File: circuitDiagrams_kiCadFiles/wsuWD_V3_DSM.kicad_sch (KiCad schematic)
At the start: 33 parts, among them J1 Conn_01x04_Male, J2 Screw Terminal, U1 MCP2561-E-P, U2 LD1086DT50TR, U3 ATmega644A-P, U7 MAX7219, U8 MCP2515-xSO, X1 ACO-20MHz-A

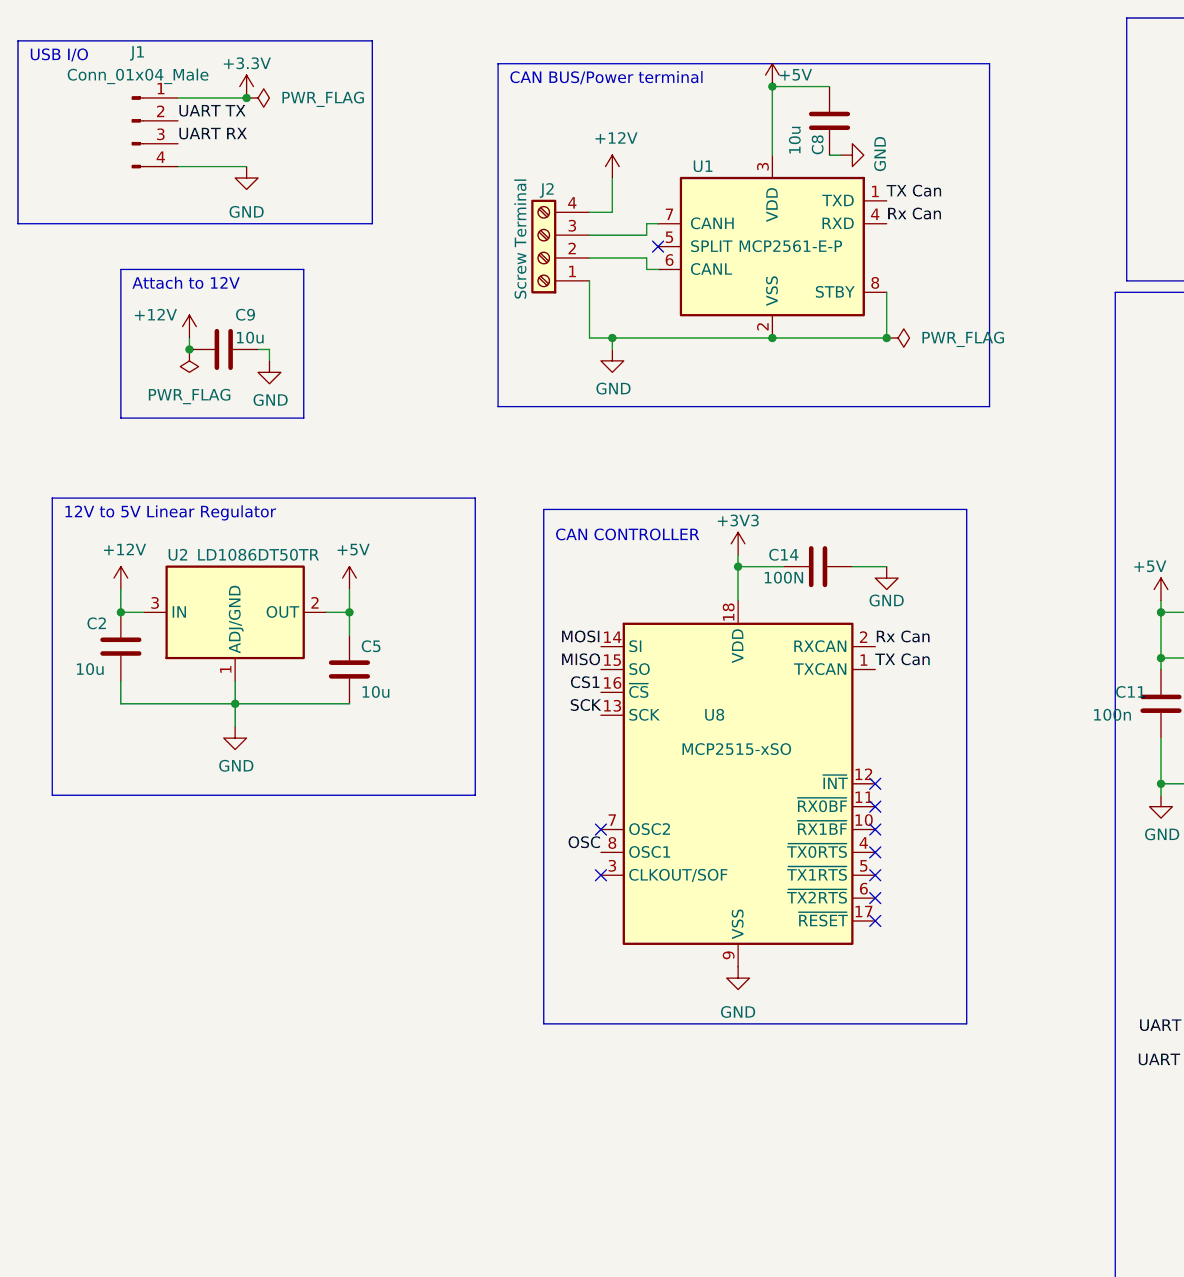
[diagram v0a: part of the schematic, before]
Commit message: Added BOB to schematic
Added BOB to schematic
Now ready for pcb design
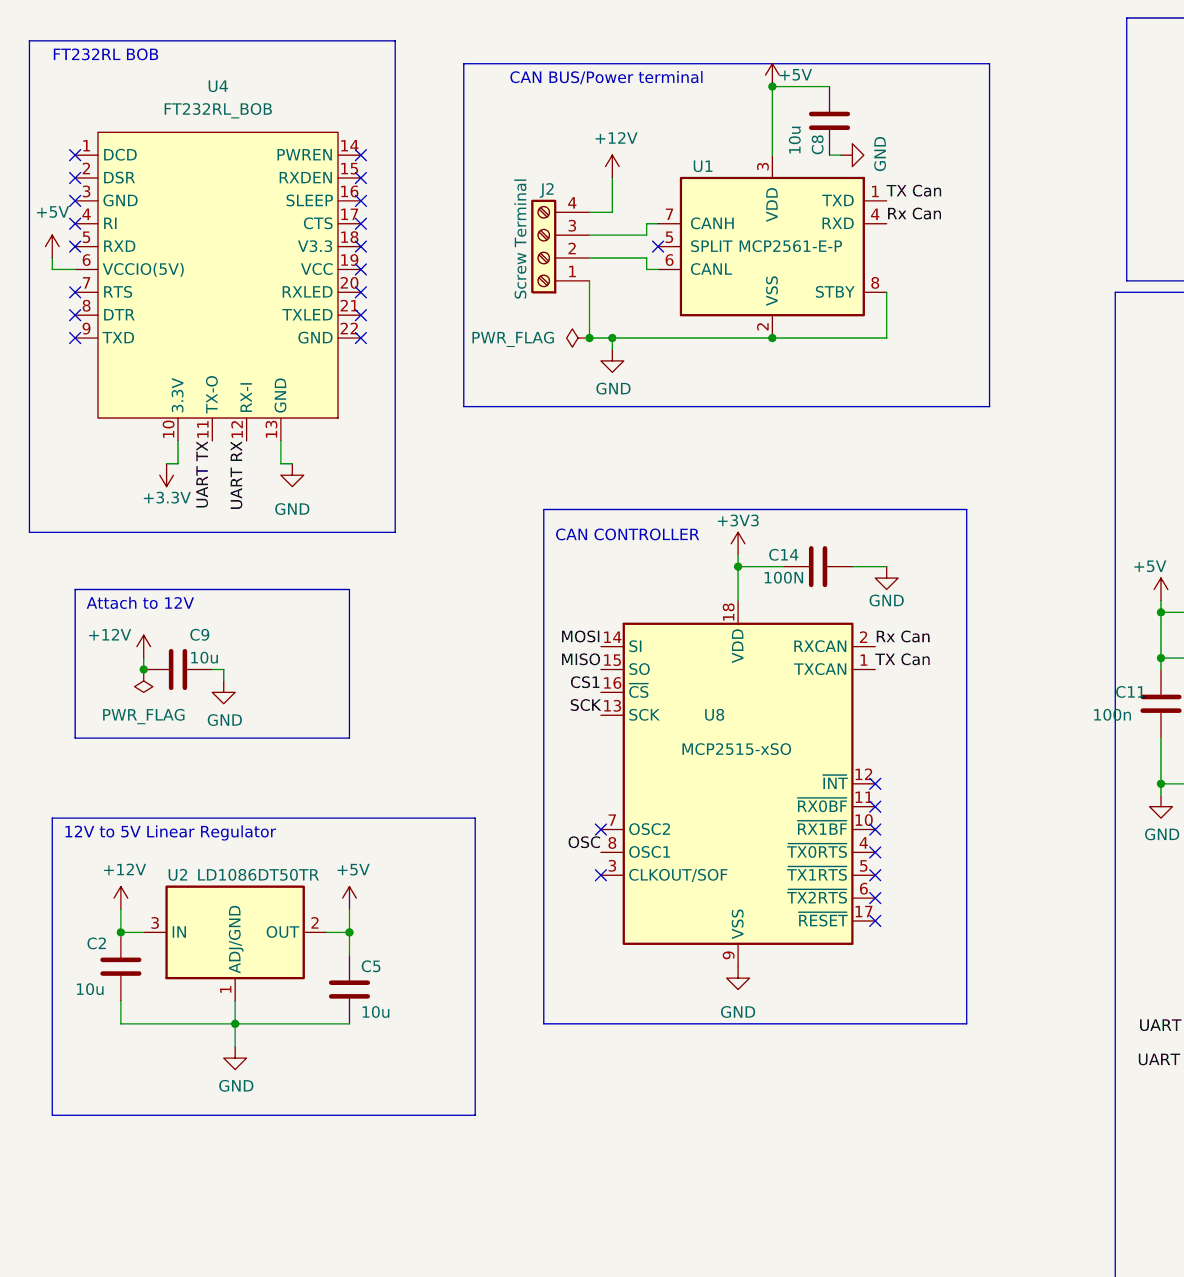
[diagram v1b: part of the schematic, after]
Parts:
- removed J1: Conn_01x04_Male, Connector_PinHeader_2.54mm:PinHeader_1x04_P2.54mm_Vertical, symbol Connector:Conn_01x04_Male
- added U4: FT232RL_BOB, Connector_PinSocket_2.54mm:PinSocket_1x05_P2.54mm_Vertical, symbol SparkFunBOB:FT232RL_BOB
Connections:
- net +3V3: now also U4.10 (3.3V)
- net +5V: now also U4.6 (VCCIO(5V))
- net GND: now also U4.13 (GND)
- net UART RX: now also U4.12 (RX-I)
- net UART TX: now also U4.11 (TX-O)
- no-connect marks 45 -> 62
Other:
- note added: "FT232RL BOB"
- note removed: "USB I/O"
- moved on the sheet: C2, C5, C9, U2
